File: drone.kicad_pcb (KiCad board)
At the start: 2 copper layers, 117.4 x 117.4 mm, 49 parts, among them J2 Conn_01x02, J3 Conn_01x02, J4 Conn_01x02, J5 Conn_01x02, J6 Conn_01x02, J7 USB_B_Micro, Q1 Si2319CDS, Q2 Si2319CDS, Q3 Si2319CDS, Q4 Si2319CDS, Q5 BSS138, Q6 BSS138, U1 ESP32-WROOM-32, U2 MPU-6050, U3 DWM1000, U4 BMP280, U5 LM1117MP-3.3, U6 CH340C

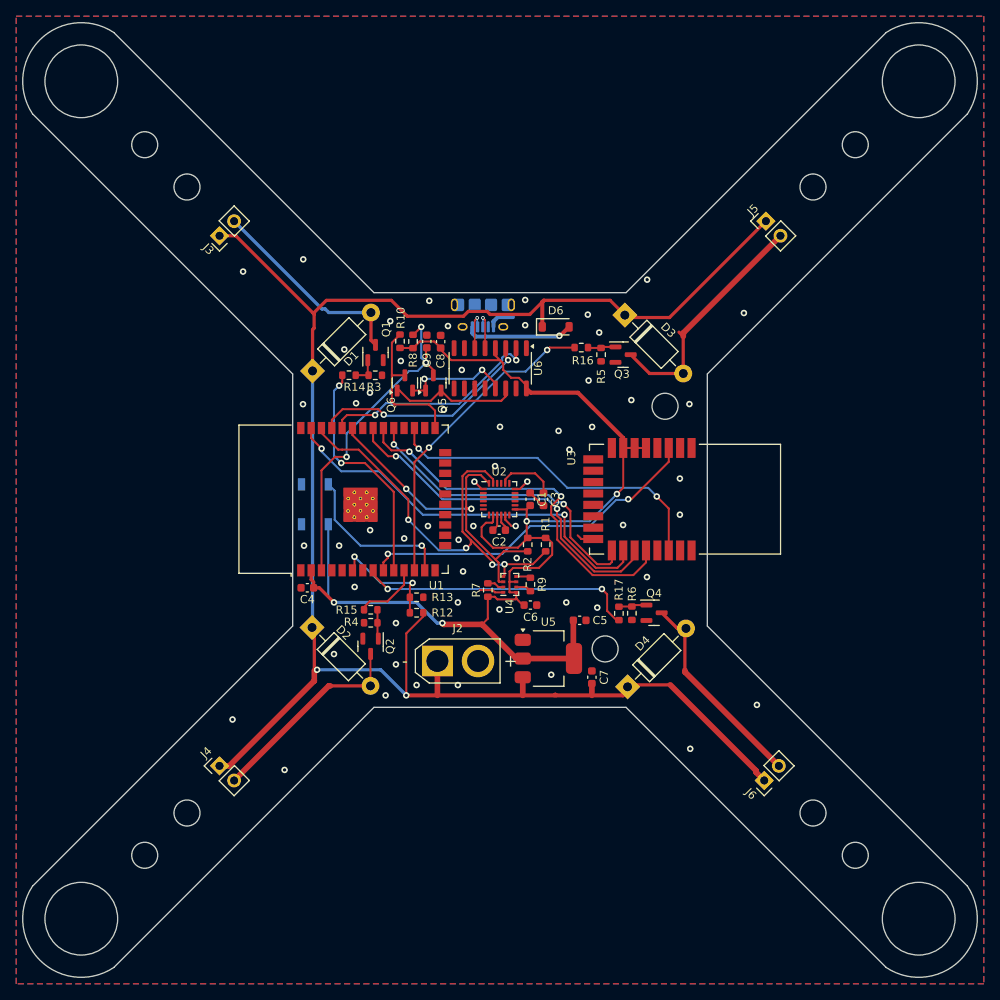
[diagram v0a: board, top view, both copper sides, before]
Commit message: bigger battery wiring
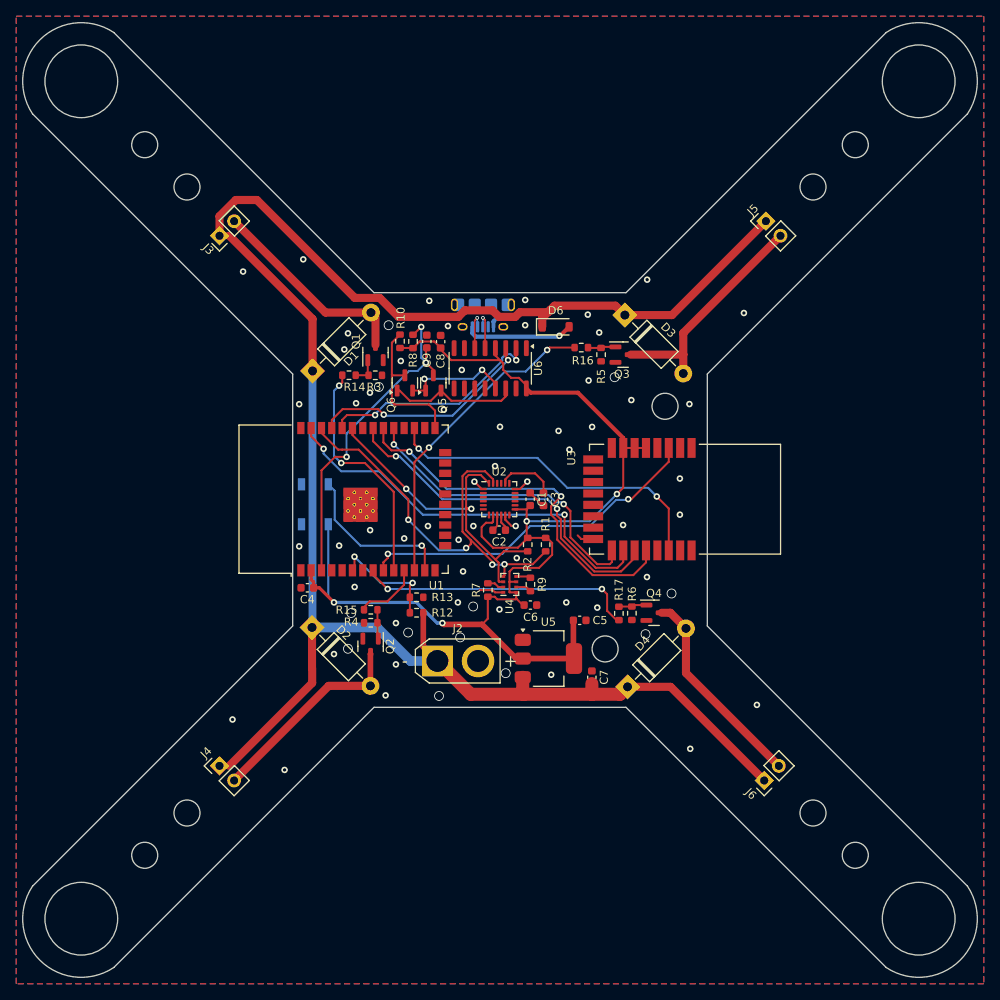
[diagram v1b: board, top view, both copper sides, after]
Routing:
- net BAT+: track 226.3 -> 238.2 mm, vias 2 -> 0
- net Net-(D3-A): track 30.1 -> 28.4 mm
- net GND: vias 58 -> 68

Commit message: add magnetometer + resive to max 10x10cm
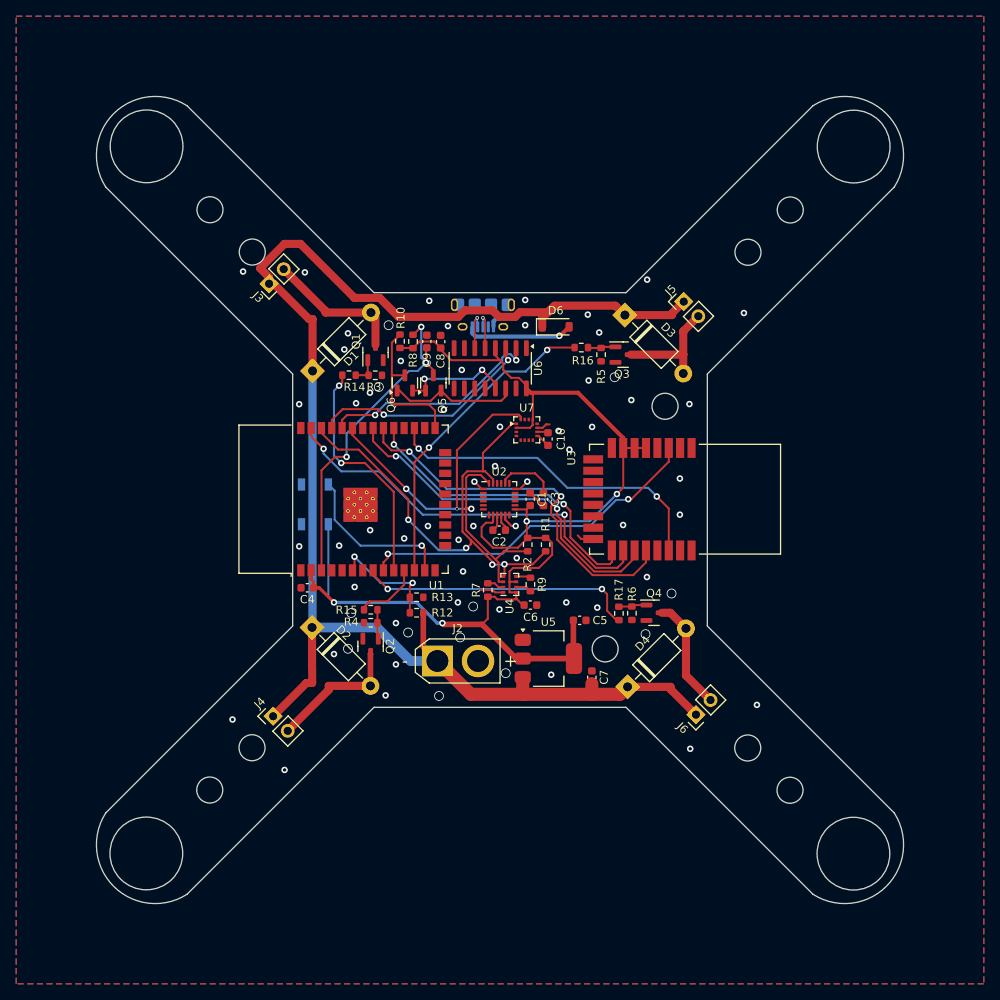
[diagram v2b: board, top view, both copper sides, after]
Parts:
- added C10: C, Capacitor_SMD:C_0603_1608Metric, F.Cu at (106.4, 93.0)
- added U7: MMC5883MA, Package_LGA:LGA-16_3x3mm_P0.5mm, F.Cu at (103.8, 91.9)
- moved J5 14.1 mm to (123.1, 76.1)
- moved J6 11.7 mm to (124.6, 126.9)
- moved J4 8.99 mm to (72.6, 127.1)
- moved J3 8.49 mm to (72.1, 73.9)
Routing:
- net BAT+: track 238.2 -> 188.0 mm
- net SDA: track 42.7 -> 60.0 mm, vias 2 -> 3
- net Net-(D3-A): track 28.4 -> 14.3 mm
- net Net-(D4-A): track 25.6 -> 14.0 mm
- net Net-(D2-A): track 25.5 -> 16.7 mm
- net Net-(D1-A): track 26.6 -> 18.1 mm
- net SCL: track 53.5 -> 61.4 mm
- net VCC: track 151.7 -> 158.7 mm
- net GND: track 20.3 -> 23.8 mm
- net Net-(U7-CAP): track 0.00 -> 1.38 mm
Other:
- board size 117.4 x 117.4 mm -> 99.3 x 99.3 mm

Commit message: add other source code
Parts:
- moved J3 2.83 mm to (74.1, 75.9)
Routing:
- net BAT+: track 188.0 -> 181.2 mm
- net Net-(D1-A): track 18.1 -> 15.3 mm
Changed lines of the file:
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@@
 	(footprint "Connector_PinHeader_2.54mm:PinHeader_1x02_P2.54mm_Vertical"
 		(layer "F.Cu")
-		(at 72.098439 73.901562 135)
+		(at 74.098439 75.901562 135)
 		(descr "Through hole straight pin header, 1x02, 2.54mm pitch, single row")
 		(tags "Through hole pin header THT 1x02 2.54mm single row")
@@
 		(layer "User.2")
 	)
+	(gr_line
+		(start 100.4 100.3)
+		(end 100.4 49)
+		(stroke
+			(width 0.15)
+			(type default)
+		)
+		(layer "User.3")
+	)
+	(gr_line
+		(start 151.65 100.4)
+		(end 100.35 100.4)
+		(stroke
+			(width 0.15)
+			(type default)
+		)
+		(layer "User.3")
+	)
+	(gr_line
+		(start 100.4 100.4)
+		(end 49.1 100.4)
+		(stroke
+			(width 0.15)
+			(type default)
+		)
+		(layer "User.3")
+	)
+	(gr_line
+		(start 100.4 151.55)
+		(end 100.4 100.25)
+		(stroke
+			(width 0.15)
+			(type default)
+		)
+		(layer "User.3")
+	)
+	(gr_line
+		(start 100.4 183.2)
+		(end 100.4 131.9)
+		(stroke
+			(width 0.15)
+			(type default)
+		)
+		(layer "User.3")
+	)
 	(segment
 		(start 100.65 103.2662)
@@
 	)
 	(segment
+		(start 75.89449 74.105511)
+		(end 79.034594 77.245615)
+		(width 1)
+		(layer "F.Cu")
+		(net 3)
+	)
+	(segment
 		(start 85.184934 78.000729)
 		(end 84.626697 77.442492)
@@
 	)
 	(segment
-		(start 79.034594 77.245615)
-		(end 73.89449 72.105511)
-		(width 1)
-		(layer "F.Cu")
-		(net 3)
-	)
-	(segment
 		(start 79.034594 77.442492)
 		(end 84.626697 77.442492)
@@
 	)
 	(segment
-		(start 79.034594 77.442492)
-		(end 79.034594 77.245615)
+		(start 85.184934 81.422496)
+		(end 85.184934 78.000729)
 		(width 1)
 		(layer "F.Cu")
@@
 	)
 	(segment
-		(start 85.184934 81.422496)
-		(end 85.184934 78.000729)
+		(start 79.034594 77.245615)
+		(end 79.034594 77.442492)
 		(width 1)
 		(layer "F.Cu")
@@
 	)
 	(via
-		(at 94.1 79.1)
+		(at 94.3 79.4)
 		(size 0.8)
 		(drill 0.4)
@@
 	)
 	(segment
+		(start 102.949275 77.4)
+		(end 106.4 77.4)
+		(width 1)
+		(layer "F.Cu")
+		(net 70)
+	)
+	(segment
+		(start 77.442492 84.626697)
+		(end 77.442492 79.442492)
+		(width 1)
+		(layer "F.Cu")
+		(net 70)
+	)
+	(segment
+		(start 75.5 76.740821)
+		(end 74.659179 75.9)
+		(width 1)
+		(layer "F.Cu")
+		(net 70)
+	)
+	(segment
+		(start 99.575 77.175)
+		(end 100.375 77.975)
+		(width 1)
+		(layer "F.Cu")
+		(net 70)
+	)
+	(segment
+		(start 77.442492 79.442492)
+		(end 75.5 77.5)
+		(width 1)
+		(layer "F.Cu")
+		(net 70)
+	)
+	(segment
 		(start 116.435224 123.236286)
 		(end 116.190235 123.481275)
@@
 	)
 	(segment
-		(start 115.857898 77.757898)
-		(end 121.65 77.757898)
+		(start 74.098439 72.901561)
+		(end 76 71)
 		(width 1)
 		(layer "F.Cu")
@@
 	)
 	(segment
-		(start 102.374275 77.975)
-		(end 100.375 77.975)
+		(start 115.857898 77.757898)
+		(end 121.65 77.757898)
 		(width 1)
 		(layer "F.Cu")
@@
 	)
 	(segment
-		(start 96.174275 77.175)
-		(end 95.374275 77.975)
+		(start 75.5 77.5)
+		(end 75.5 76.740821)
 		(width 1)
 		(layer "F.Cu")
@@
 	)
 	(segment
-		(start 74 69)
-		(end 71 72)
-		(width 1)
-		(layer "F.Cu")
-		(net 70)
-	)
-	(segment
-		(start 106.7 77.1)
-		(end 106.4 77.4)
+		(start 82.598127 75.642492)
+		(end 85.698127 75.642492)
 		(width 1)
 		(layer "F.Cu")
@@
 	)
 	(segment
-		(start 95.374275 77.975)
-		(end 88.030635 77.975)
+		(start 88.030635 77.975)
+		(end 95.374275 77.975)
 		(width 1)
 		(layer "F.Cu")
@@
 	)
 	(segment
-		(start 100.375 77.975)
-		(end 99.575 77.175)
-		(width 1)
+		(start 103.3 124.3)
+		(end 103.4 124.4)
+		(width 1.6)
 		(layer "F.Cu")
 		(net 70)
 	)
 	(segment
-		(start 75.955635 69)
-		(end 74 69)
+		(start 105.7 79.2)
+		(end 105.7 78.1)
 		(width 1)
 		(layer "F.Cu")
@@
 	)
 	(segment
-		(start 103.3 124.3)
-		(end 103.4 124.4)
-		(width 1.6)
+		(start 116.190235 123.979765)
+		(end 115.64 124.53)
+		(width 0.5)
 		(layer "F.Cu")
 		(net 70)
 	)
 	(segment
-		(start 99.575 77.175)
-		(end 96.174275 77.175)
+		(start 121.481275 123.481275)
+		(end 116.190235 123.481275)
 		(width 1)
 		(layer "F.Cu")
@@
 	)
 	(segment
-		(start 105.7 79.2)
-		(end 105.7 78.1)
+		(start 105.7 78.1)
+		(end 106.7 77.1)
 		(width 1)
 		(layer "F.Cu")
@@
 	)
 	(segment
-		(start 71 72)
-		(end 72.098439 73.098439)
-		(width 1)
+		(start 103.4 124.4)
+		(end 111.8 124.4)
+		(width 1.6)
 		(layer "F.Cu")
 		(net 70)
 	)
 	(segment
-		(start 72.660741 73.901562)
-		(end 72.098439 73.901562)
+		(start 106.7 77.1)
+		(end 107.2 76.6)
 		(width 1)
 		(layer "F.Cu")
@@
 	)
 	(segment
-		(start 116.190235 123.979765)
-		(end 115.64 124.53)
-		(width 0.5)
+		(start 78 71)
+		(end 82.598127 75.598127)
+		(width 1)
 		(layer "F.Cu")
 		(net 70)
 	)
 	(segment
-		(start 121.481275 123.481275)
-		(end 116.190235 123.481275)
-		(width 1)
+		(start 111.8 123.075)
+		(end 111.8 124.4)
+		(width 1.6)
 		(layer "F.Cu")
 		(net 70)
 	)
 	(segment
-		(start 105.7 78.1)
+		(start 106.4 77.4)
 		(end 106.7 77.1)
 		(width 1)
@@
 	)
 	(segment
-		(start 103.4 124.4)
-		(end 111.8 124.4)
-		(width 1.6)
+		(start 77.4 123.006031)
+		(end 77.4 121.216931)
+		(width 1)
 		(layer "F.Cu")
 		(net 70)
 	)
 	(segment
-		(start 106.7 77.1)
-		(end 107.2 76.6)
+		(start 82.598127 75.598127)
+		(end 82.598127 75.642492)
 		(width 1)
 		(layer "F.Cu")
@@
 	)
 	(segment
-		(start 111.8 123.075)
-		(end 111.8 124.4)
-		(width 1.6)
+		(start 85.698127 75.642492)
+		(end 88.030635 77.975)
+		(width 1)
 		(layer "F.Cu")
 		(net 70)
 	)
 	(segment
-		(start 77.4 123.006031)
-		(end 77.4 121.216931)
+		(start 100.375 77.975)
+		(end 102.374275 77.975)
 		(width 1)
 		(layer "F.Cu")
@@
 	)
 	(segment
-		(start 77.442492 84.626697)
-		(end 77.442492 78.24041)
+		(start 74.659179 75.9)
+		(end 74.098439 75.9)
 		(width 1)
 		(layer "F.Cu")
@@
 	)
 	(segment
-		(start 77.442492 78.24041)
-		(end 76.999589 78.24041)
+		(start 102.374275 77.975)
+		(end 102.949275 77.4)
 		(width 1)
 		(layer "F.Cu")
@@
 	)
 	(segment
-		(start 106.4 77.4)
-		(end 102.949275 77.4)
-		(width 1)
-		(layer "F.Cu")
-		(net 70)
-	)
-	(segment
-		(start 76.999589 78.24041)
-		(end 72.660741 73.901562)
-		(width 1)
-		(layer "F.Cu")
-		(net 70)
-	)
-	(segment
-		(start 102.949275 77.4)
-		(end 102.374275 77.975)
+		(start 96.174275 77.175)
+		(end 99.575 77.175)
 		(width 1)
 		(layer "F.Cu")
@@
 	)
 	(segment
-		(start 85.698127 75.642492)
-		(end 82.598127 75.642492)
+		(start 77.380684 121.197615)
+		(end 77.380684 116.178366)
 		(width 1)
 		(layer "F.Cu")
@@
 	)
 	(segment
-		(start 77.380684 121.197615)
-		(end 77.380684 116.178366)
+		(start 76 71)
+		(end 78 71)
 		(width 1)
 		(layer "F.Cu")
@@
 	)
 	(segment
-		(start 72.098439 73.098439)
-		(end 72.098439 73.901562)
-		(width 1)
-		(layer "F.Cu")
-		(net 70)
-	)
-	(segment
 		(start 115.27151 124.4)
 		(end 116.190235 123.481275)
@@
 	)
 	(segment
-		(start 82.598127 75.642492)
-		(end 75.955635 69)
-		(width 1)
-		(layer "F.Cu")
-		(net 70)
-	)
-	(segment
 		(start 91.065 118.565)
 		(end 91.065 114.37)
@@
 	)
 	(segment
-		(start 121.481275 123.784398)
-		(end 121.481275 123.481275)
+		(start 74.098439 75.9)
+		(end 74.098439 72.901561)
 		(width 1)
 		(layer "F.Cu")
@@
 	)
 	(segment
-		(start 88.030635 77.975)
-		(end 85.698127 75.642492)
+		(start 121.481275 123.784398)
+		(end 121.481275 123.481275)
 		(width 1)
 		(layer "F.Cu")
@@
 		(layer "F.Cu")
 		(net 70)
+	)
+	(segment
+		(start 95.374275 77.975)
+		(end 96.174275 77.175)
+		(width 1)
+		(layer "F.Cu")
+		(net 70)

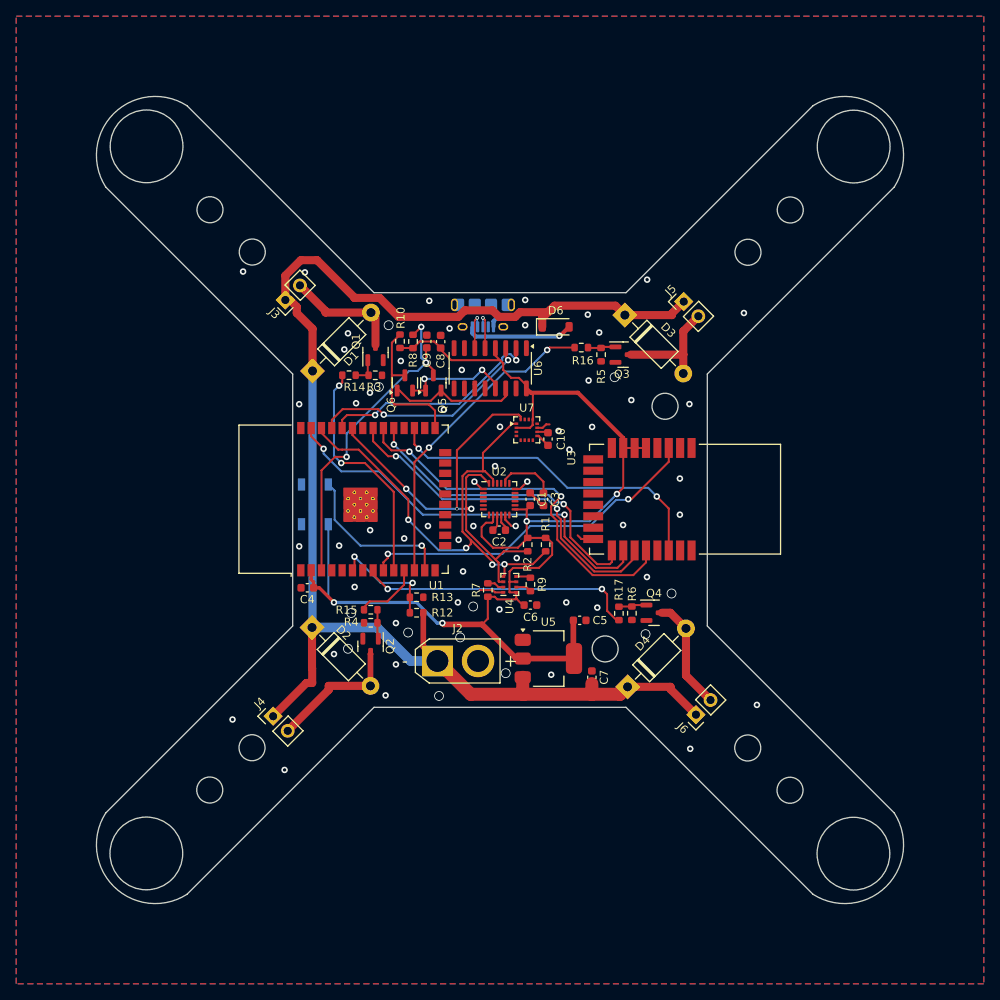
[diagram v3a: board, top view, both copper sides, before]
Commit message: pass si2301 to DRV8231
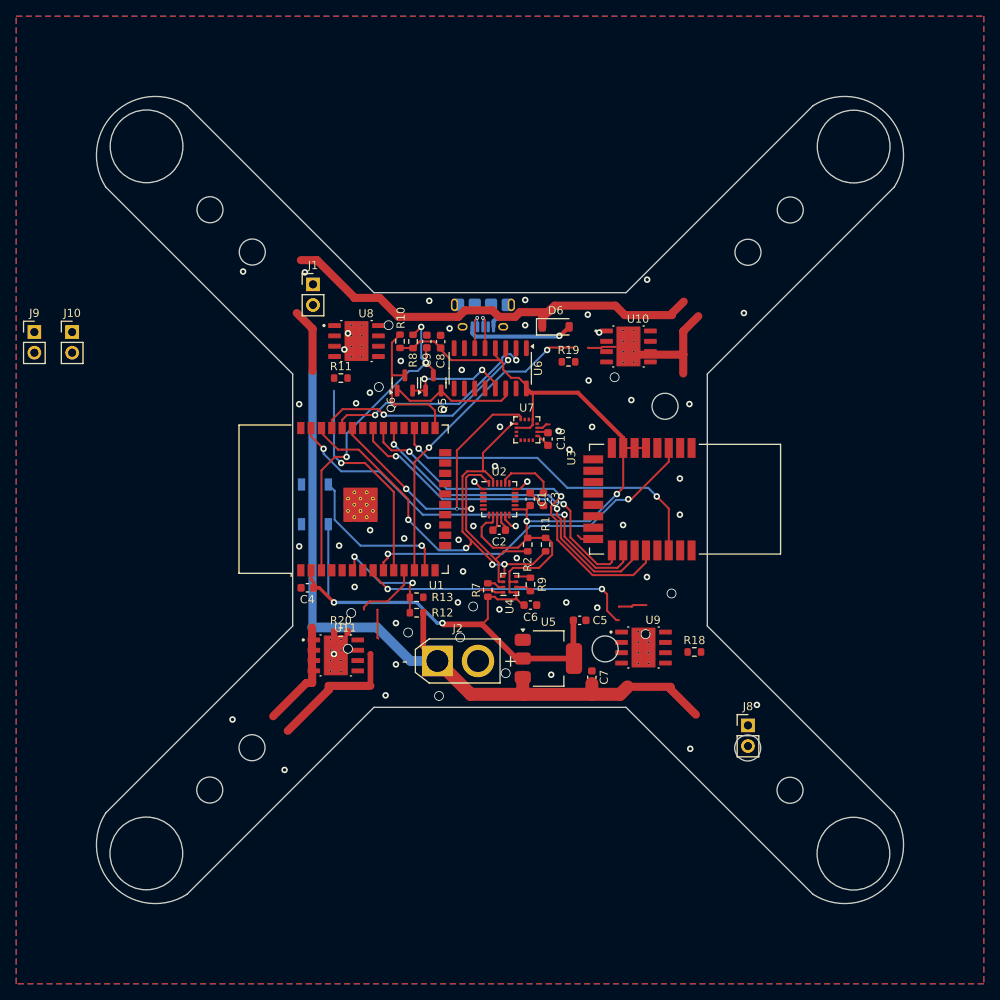
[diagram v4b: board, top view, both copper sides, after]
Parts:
- removed D1, D2, D3, D4: 1N5819, Diode_THT:D_DO-41_SOD81_P10.16mm_Horizontal
- removed J3, J4, J5, J6: Conn_01x02, Connector_PinHeader_2.54mm:PinHeader_1x02_P2.54mm_Vertical
- removed Q1, Q2, Q3, Q4: Si2319CDS, Package_TO_SOT_SMD:SOT-23
- removed R14, R15, R16, R17, R3, R4, R5, R6: R_Small, Resistor_SMD:R_0603_1608Metric
- added J1: Conn_01x02, Connector_PinHeader_2.54mm:PinHeader_1x02_P2.54mm_Vertical, F.Cu at (77.5, 74.0)
- added J10: Conn_01x02, Connector_PinHeader_2.54mm:PinHeader_1x02_P2.54mm_Vertical, F.Cu at (47.9, 79.8)
- added J8: Conn_01x02, Connector_PinHeader_2.54mm:PinHeader_1x02_P2.54mm_Vertical, F.Cu at (131.0, 128.2)
- added J9: Conn_01x02, Connector_PinHeader_2.54mm:PinHeader_1x02_P2.54mm_Vertical, F.Cu at (43.2, 79.8)
- added R11: R_Small, Resistor_SMD:R_0603_1608Metric, F.Cu at (80.9, 85.5)
- added R18: R_Small, Resistor_SMD:R_0603_1608Metric, F.Cu at (124.4, 119.2)
- added R19: R_Small, Resistor_SMD:R_0603_1608Metric, F.Cu at (108.9, 83.5)
- added R20: R_Small, Resistor_SMD:R_0603_1608Metric, F.Cu at (80.9, 116.8)
- added U10: DRV8231DDAR, DRV8231:IC_DRV8231DDAR, F.Cu at (116.3, 81.6)
- added U11: DRV8231DDAR, DRV8231:IC_DRV8231DDAR, F.Cu at (80.3, 119.6)
- added U8: DRV8231DDAR, DRV8231:IC_DRV8231DDAR, F.Cu at (82.8, 81.0)
- added U9: DRV8231DDAR, DRV8231:IC_DRV8231DDAR, F.Cu at (118.2, 118.7)
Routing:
- net (no net): track 0.00 -> 41.5 mm
- net Net-(D2-A): track 16.7 -> 0.00 mm
- net Net-(D1-A): track 15.3 -> 0.00 mm
- net Net-(D3-A): track 14.3 -> 0.00 mm
- net Net-(D4-A): track 14.0 -> 0.00 mm
- net BAT+: track 181.2 -> 173.0 mm
- net Net-(Q2-G): track 3.60 -> 0.00 mm
- net Net-(Q4-G): track 3.51 -> 0.00 mm
- net Net-(Q1-G): track 3.49 -> 0.00 mm
- net Net-(Q3-G): track 3.45 -> 0.00 mm
- net MOTOR_1: track 29.2 -> 26.8 mm, vias 2 -> 1
